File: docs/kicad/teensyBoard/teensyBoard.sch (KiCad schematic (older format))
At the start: 6 parts

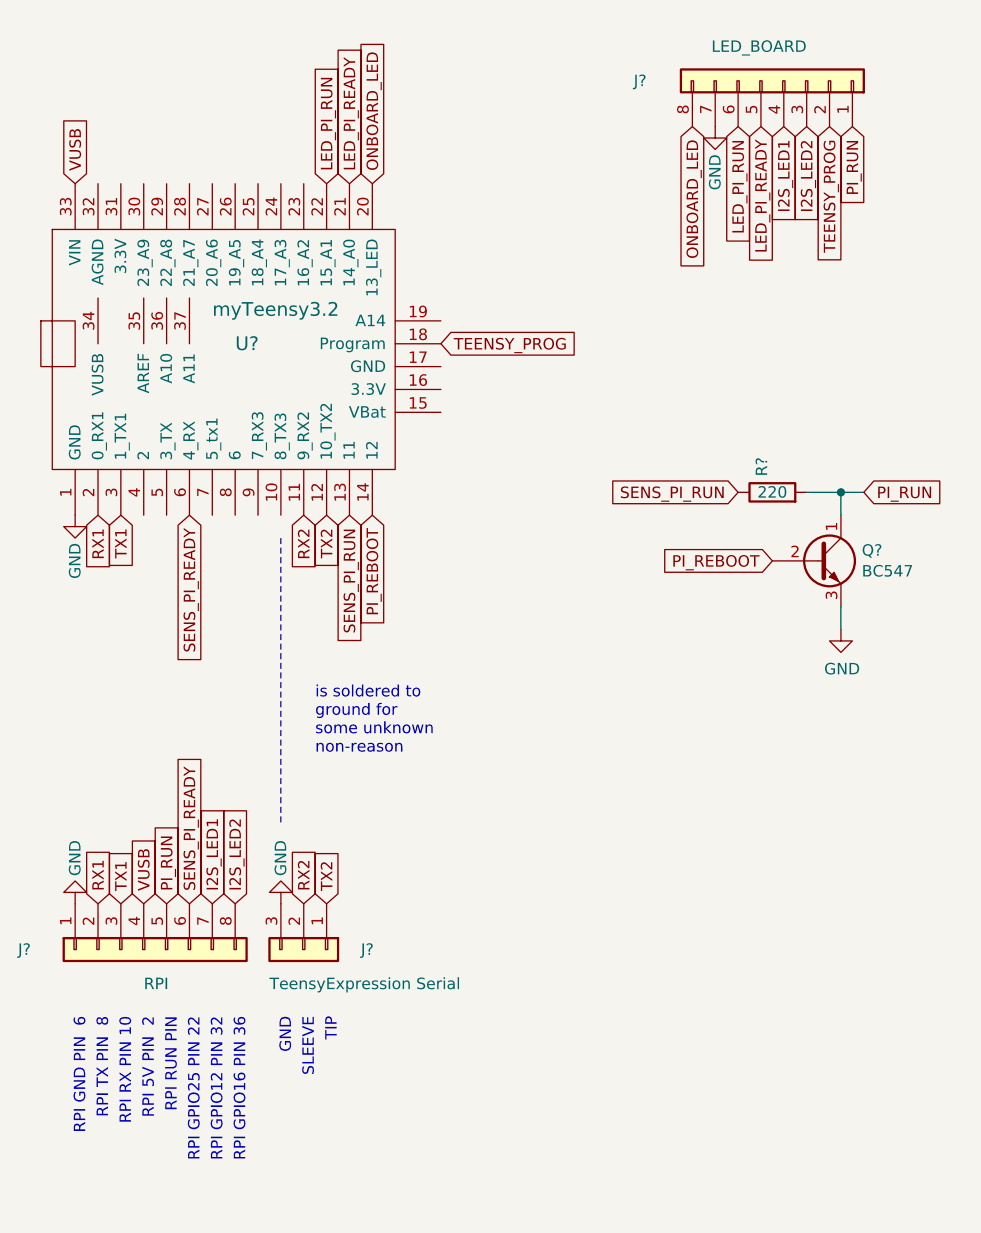
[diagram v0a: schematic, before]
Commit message: docs - update/add more text labels for buttons and leds to schematics
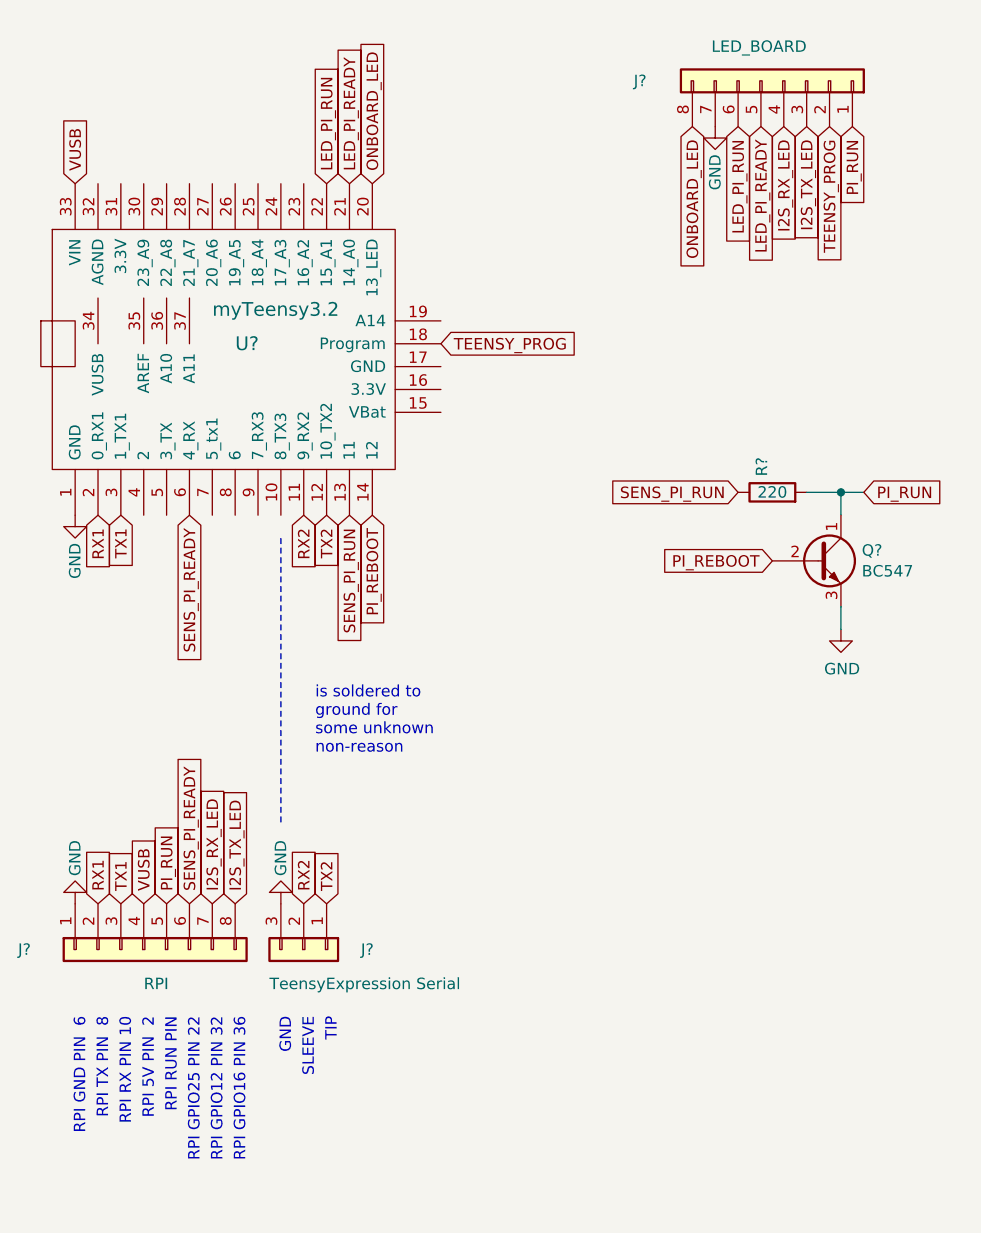
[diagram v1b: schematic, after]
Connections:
- net I2S_LED1 renamed I2S_RX_LED
- net I2S_LED2 renamed I2S_TX_LED
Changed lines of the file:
@@
 Text GLabel 5100 2150 1    50   Input ~ 0
 LED_PI_READY
-Text GLabel 4600 5300 1    50   Input ~ 0
-I2S_LED2
 Text GLabel 4500 5300 1    50   Input ~ 0
-I2S_LED1
+I2S_RX_LED
 Text GLabel 3900 2150 1    50   Input ~ 0
 VUSB
@@
 LED_PI_READY
 Text GLabel 7000 1900 3    50   Input ~ 0
-I2S_LED1
-Text GLabel 7100 1900 3    50   Input ~ 0
-I2S_LED2
+I2S_RX_LED
 $Comp
 L power:GND #PWR?
@@
 Text Notes 5050 5800 3    50   ~ 0
 TIP
+Text GLabel 4600 5300 1    50   Input ~ 0
+I2S_TX_LED
+Text GLabel 7100 1900 3    50   Input ~ 0
+I2S_TX_LED
 $EndSCHEMATC
